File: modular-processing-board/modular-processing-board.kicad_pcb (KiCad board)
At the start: 6 copper layers, 90 x 90 mm, 159 parts, among them J202 Conn_02x06_Odd_Even, J401 Micro_SD_Card, J501 Plug_Hirose_DF40_2x40_DF40C-8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, J502 Conn_02x06_Odd_Even, J601 Conn_Coaxial_Small, J604 Conn_Coaxial_Small, J701 Conn_02x02_Odd_Even, J801 TYPE-C-31-M-12, SW201 SW_Push, SW602 SW_Push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

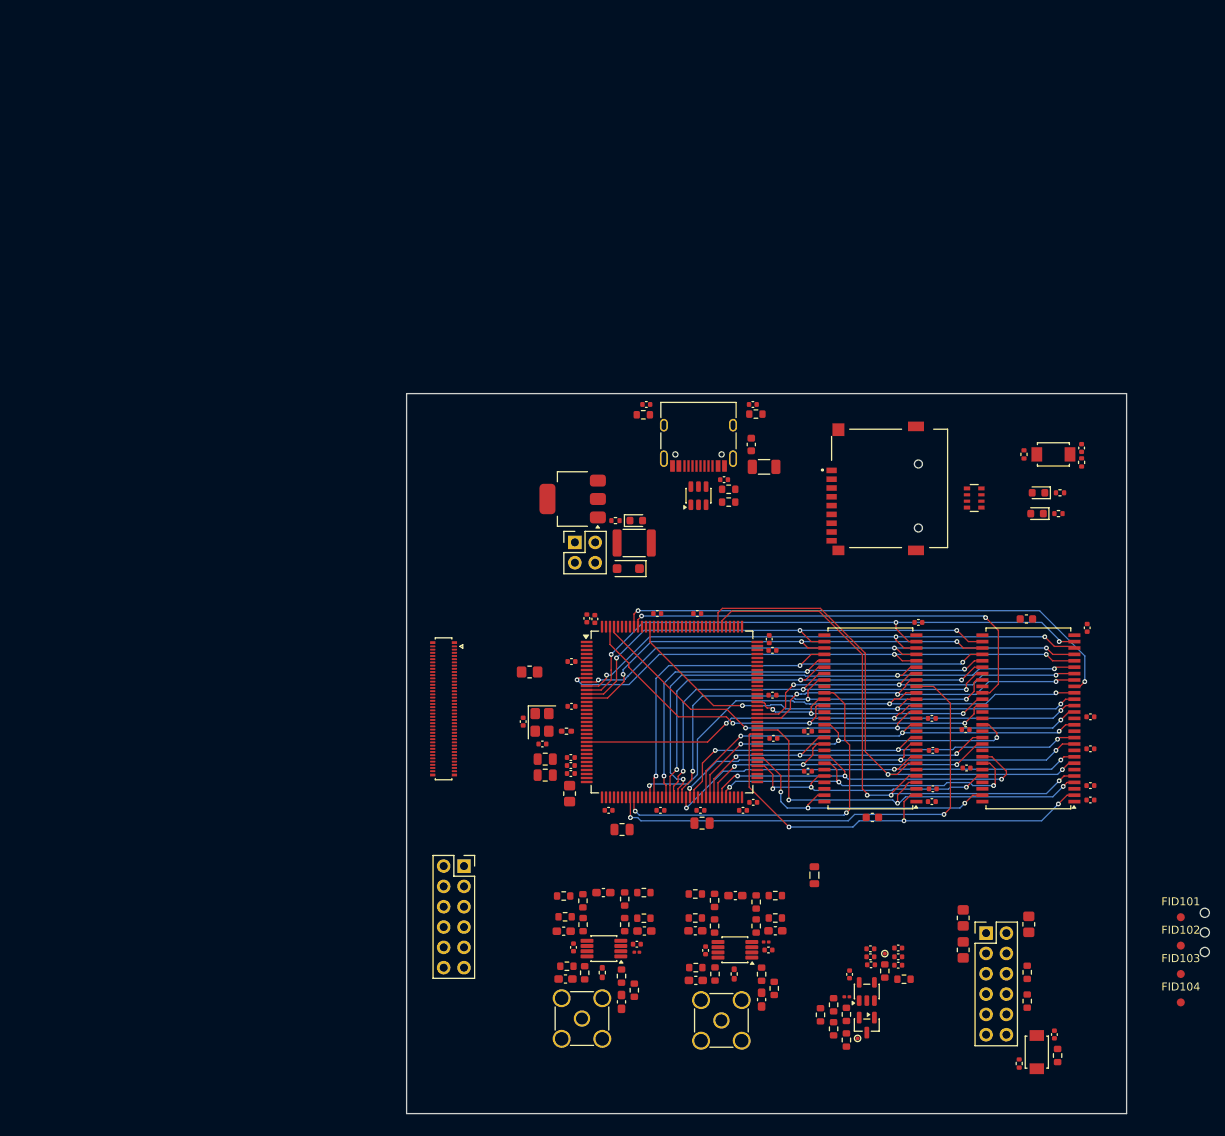
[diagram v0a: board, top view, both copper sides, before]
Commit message: checked timing for sdram, routing
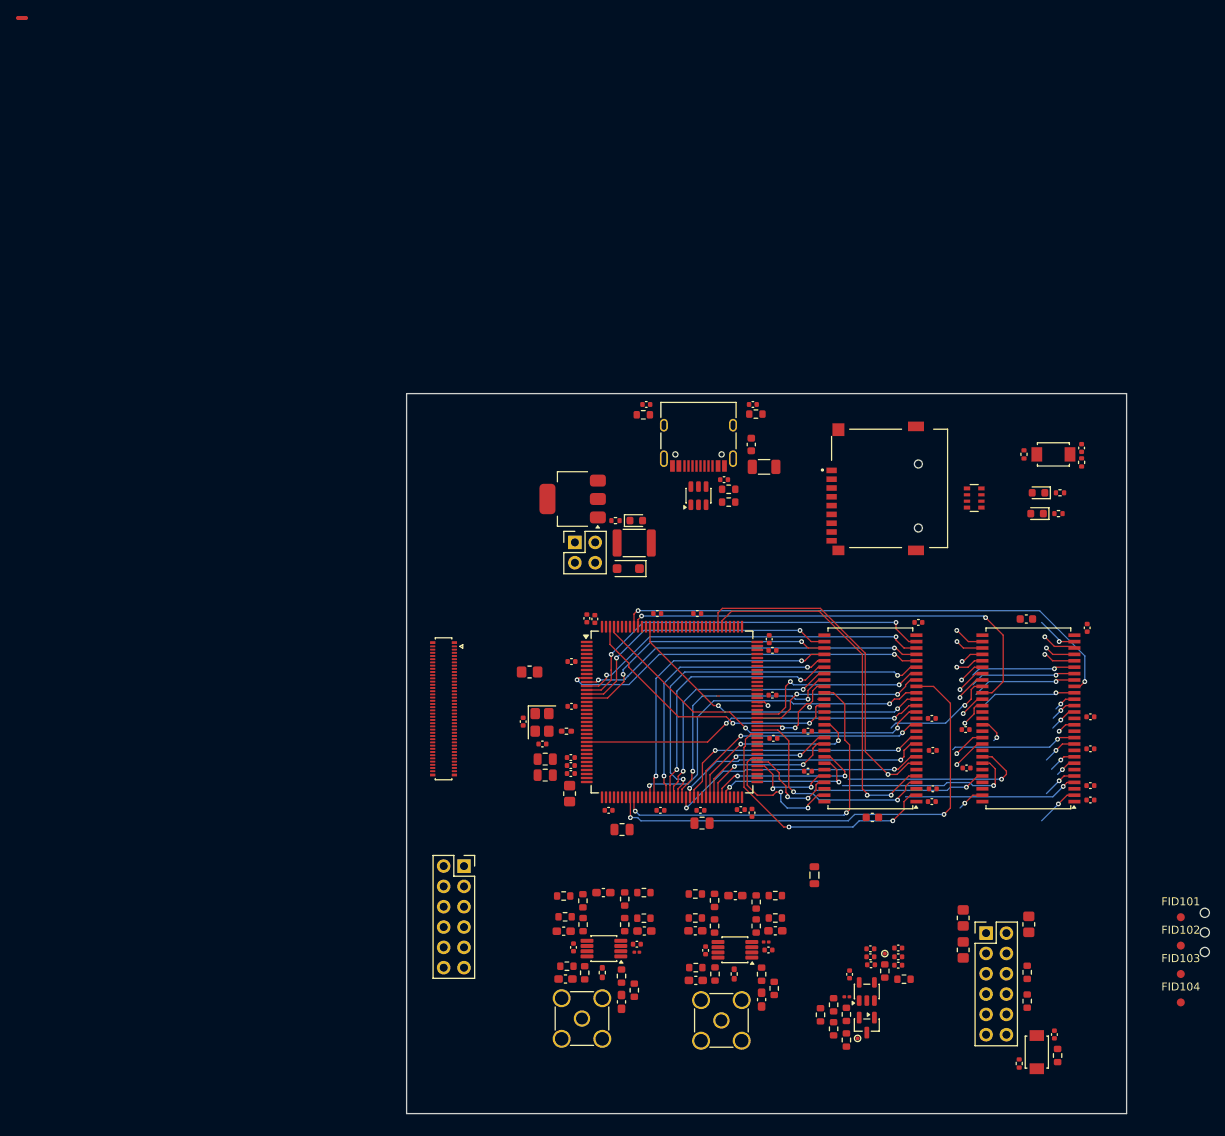
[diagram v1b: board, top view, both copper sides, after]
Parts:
- added NT301: NetTie_2, NetTie:NetTie-2_SMD_Pad0.5mm, F.Cu at (0.75, 0.25)
- moved C211 1.32 mm to (92.0, 99.6), turned to 90 degrees
- moved C222 0.29 mm to (90.6, 99.2)
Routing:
- net /mcu/SDRAM.A12: track 0.00 -> 26.6 mm, vias 0 -> 3
- net /mcu/SDRAM.D3: track 67.0 -> 45.8 mm
- net /mcu/SDRAM.A6: track 60.7 -> 40.3 mm
- net /mcu/SDRAM.A9: track 55.2 -> 35.1 mm
- net /mcu/SDRAM.~{WE}: track 66.3 -> 46.4 mm
- net /mcu/SDRAM.A8: track 56.5 -> 36.7 mm
- net /mcu/SDRAM.A11: track 54.2 -> 34.6 mm
- net /mcu/SDRAM.D4: track 55.9 -> 36.3 mm
- net /mcu/SDRAM.A4: track 58.5 -> 38.9 mm
- net /mcu/SDRAM.~{CAS}: track 61.9 -> 42.3 mm
- net /mcu/SDRAM.D2: track 70.0 -> 50.5 mm
- net /mcu/SDRAM.D8: track 46.5 -> 27.1 mm
- net /mcu/SDRAM.A5: track 56.9 -> 37.5 mm
- net /mcu/SDRAM.D9: track 42.0 -> 22.6 mm
- net /mcu/SDRAM.UDQM: track 58.0 -> 38.6 mm
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
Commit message: rough length mamatching for sdram (next) route PSSI-bus
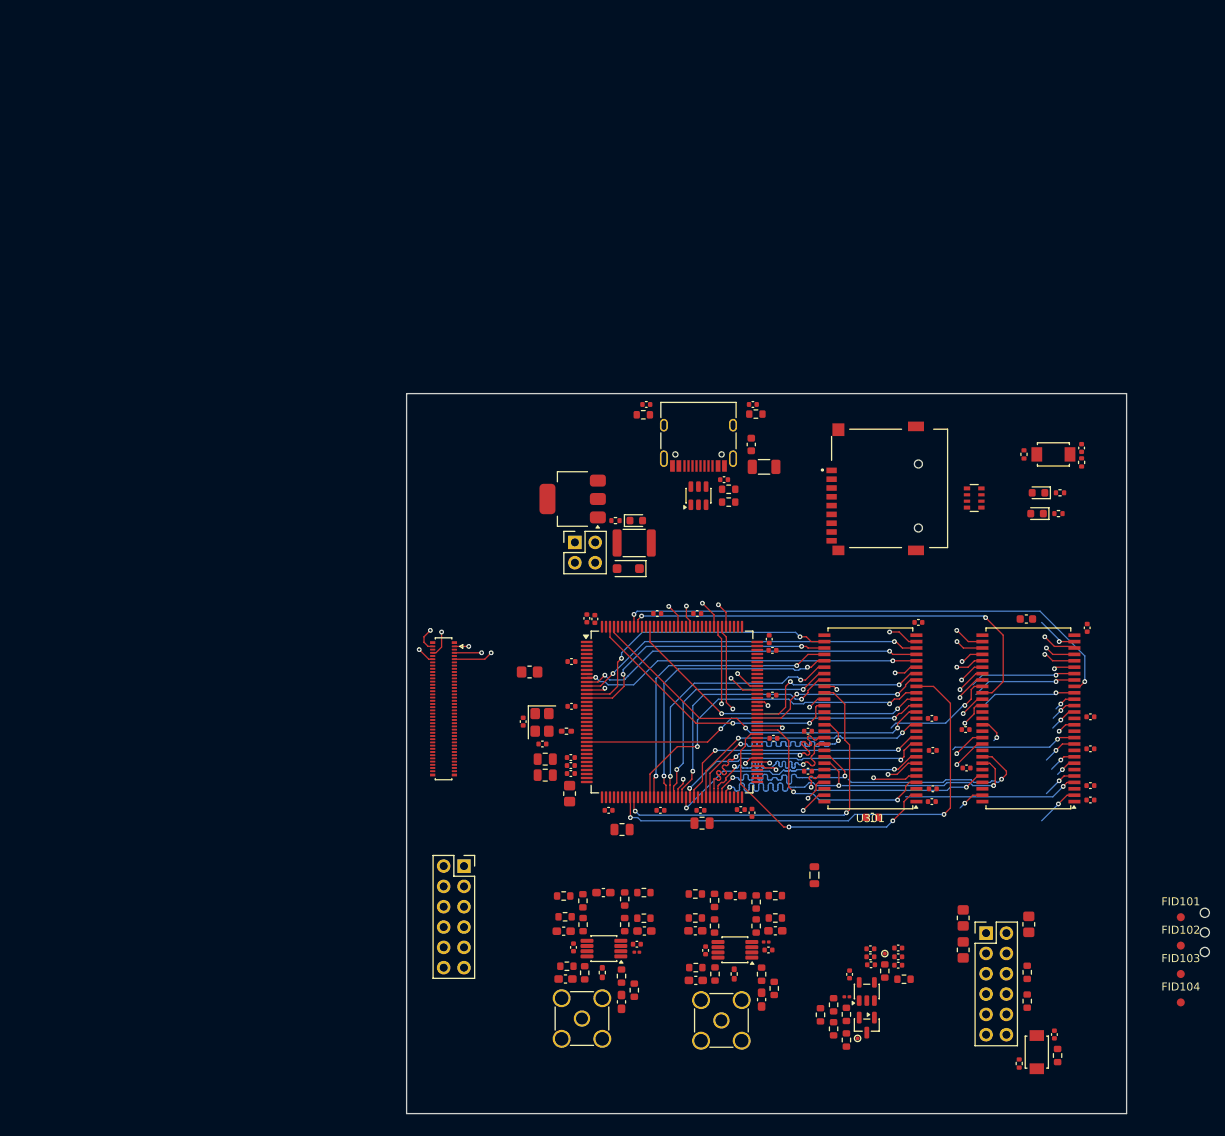
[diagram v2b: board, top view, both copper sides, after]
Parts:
- removed NT301: NetTie_2, NetTie:NetTie-2_SMD_Pad0.5mm
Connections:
- J501 pad 11: Net-(J501-Pad11) -> GND
- J501 pad 12: Net-(J501-Pad12) -> GND
- J501 pad 15: Net-(J501-Pad11) -> GND
- J501 pad 16: Net-(J501-Pad12) -> GND
- J501 pad 19: Net-(J501-Pad11) -> GND
- J501 pad 20: Net-(J501-Pad12) -> GND
- J501 pad 23: Net-(J501-Pad11) -> GND
- J501 pad 24: Net-(J501-Pad12) -> GND
- J501 pad 27: Net-(J501-Pad11) -> GND
- J501 pad 28: Net-(J501-Pad12) -> GND
- J501 pad 3: Net-(J501-Pad11) -> GND
- J501 pad 31: Net-(J501-Pad11) -> GND
- J501 pad 32: Net-(J501-Pad12) -> GND
- J501 pad 35: Net-(J501-Pad11) -> GND
- J501 pad 36: Net-(J501-Pad12) -> GND
- J501 pad 39: Net-(J501-Pad11) -> GND
- J501 pad 4: Net-(J501-Pad12) -> GND
- J501 pad 40: Net-(J501-Pad12) -> GND
- J501 pad 43: Net-(J501-Pad11) -> GND
- J501 pad 44: Net-(J501-Pad12) -> GND
- J501 pad 47: Net-(J501-Pad11) -> GND
- J501 pad 48: Net-(J501-Pad12) -> GND
- J501 pad 7: Net-(J501-Pad11) -> GND
- J501 pad 8: Net-(J501-Pad12) -> GND
- U201 pad 125: unconnected-(U201-PG10-Pad125) -> /connectors/PSSI.D2
- U201 pad 98: /connectors/PSSI.D2 -> unconnected-(U201-PC8-Pad98)
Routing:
- net /connectors/PSSI.D9: track 0.00 -> 44.9 mm, vias 0 -> 2
- net /connectors/PSSI.D11: track 0.00 -> 44.3 mm, vias 0 -> 2
- net /connectors/PSSI.D0: track 0.00 -> 42.3 mm, vias 0 -> 2
- net /connectors/PSSI.D1: track 0.00 -> 41.6 mm, vias 0 -> 2
- net /connectors/PSSI.D10: track 0.00 -> 38.5 mm, vias 0 -> 2
- net /connectors/PSSI.D2: track 0.00 -> 32.5 mm, vias 0 -> 2
- net /mcu/SDRAM.CLK: track 27.4 -> 44.9 mm
- net /mcu/SDRAM.A10: track 60.5 -> 43.4 mm
- net /mcu/SDRAM.D14: track 12.6 -> 28.4 mm
- net /mcu/SDRAM.A12: track 26.6 -> 41.7 mm
- net /mcu/SDRAM.D15: track 20.6 -> 35.6 mm
- net /mcu/SDRAM.D13: track 34.2 -> 48.8 mm
- net /mcu/SDRAM.D10: track 21.9 -> 30.9 mm
- net /mcu/SDRAM.D12: track 42.3 -> 51.1 mm
- net /mcu/SDRAM.D2: track 50.5 -> 42.0 mm
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
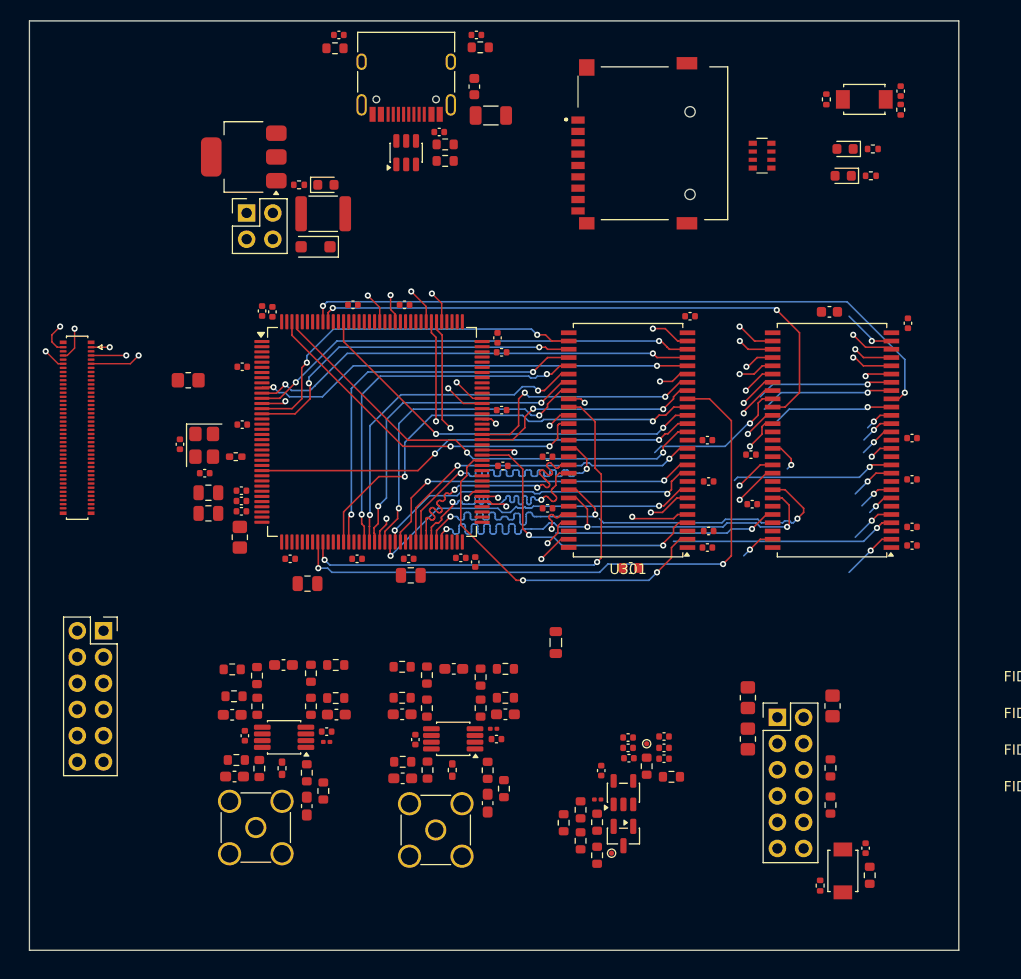
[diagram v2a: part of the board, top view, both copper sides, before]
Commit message: replaced sdmmc connector, added smmc trace, added u.fl. connectors
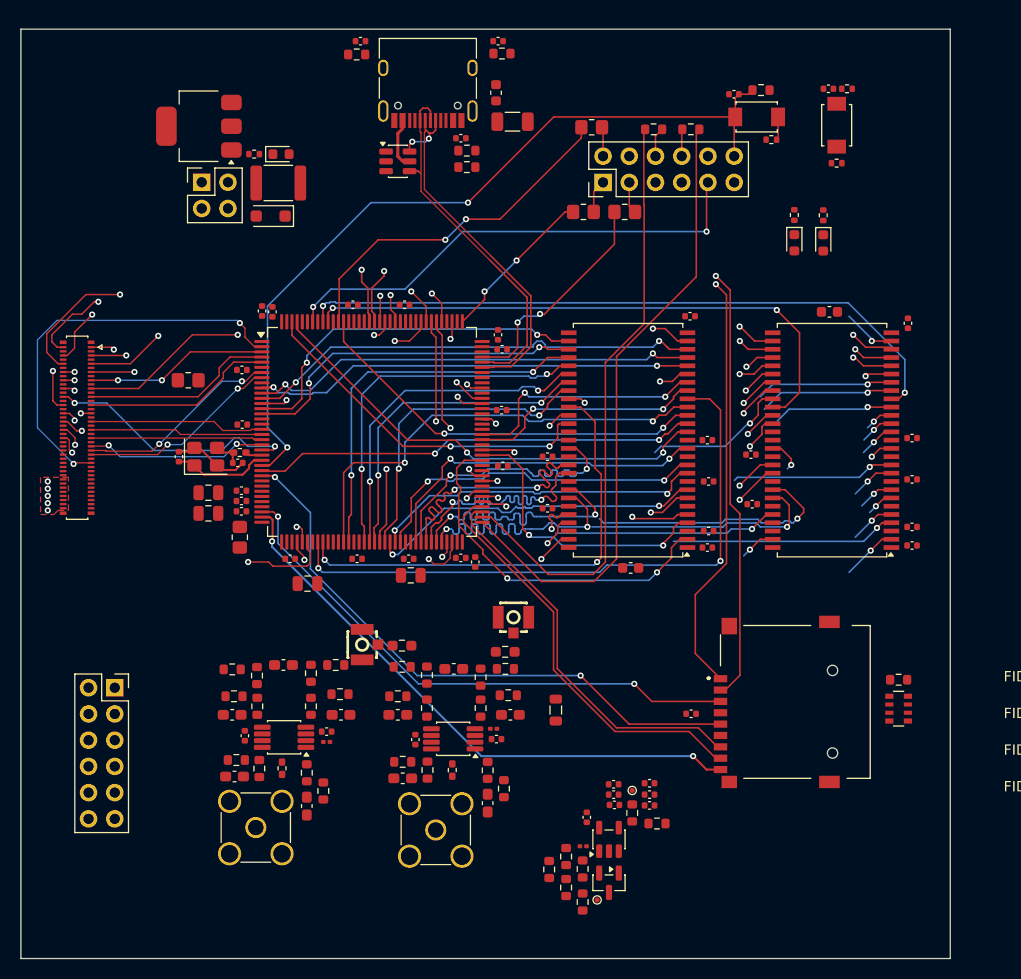
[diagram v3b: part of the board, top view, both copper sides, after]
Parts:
- added C401: 0.1uF, Capacitor_SMD:C_0402_1005Metric, F.Cu at (112.9, 114.3)
- added J1001: BWU.FL-IPEX1, iw-connector:BWU.FL-IPEX1, F.Cu at (95.7, 105.7)
- added J602: BWU.FL-IPEX1, iw-connector:BWU.FL-IPEX1, F.Cu at (81.8, 107.6)
- added R1001: 0, Resistor_SMD:R_0603_1608Metric_Pad0.98x0.95mm_HandSolder, F.Cu at (84.9, 107.7)
- added R401: 10k, Resistor_SMD:R_0603_1608Metric, F.Cu at (133.0, 111.0)
- added R620: 0, Resistor_SMD:R_0603_1608Metric_Pad0.98x0.95mm_HandSolder, F.Cu at (94.9, 108.3)
- J401: value Micro_SD_Card -> TF01A
- moved R208 76.8 mm to (119.7, 53.9), turned to 180 degrees
- moved C216 74.1 mm to (117.0, 54.3), turned to 180 degrees
- moved SW201 73.5 mm to (119.2, 56.5), turned to 0 degrees
- moved R216 72.4 mm to (120.7, 58.7), turned to 180 degrees
- moved R215 66.8 mm to (112.9, 57.7), turned to 180 degrees
- moved R214 64.2 mm to (109.3, 57.7), turned to 0 degrees
- moved R207 60.7 mm to (103.3, 57.5), turned to 0 degrees
- moved J401 55.8 mm to (123.0, 113.2)
- moved RN707 55.2 mm to (133.0, 113.8), turned to 0 degrees
- moved J202 54.5 mm to (104.4, 62.8), turned to 90 degrees
- moved R218 52.4 mm to (106.5, 65.7), turned to 180 degrees
- moved R217 49.7 mm to (102.5, 65.7), turned to 180 degrees
- moved D401 10.3 mm to (122.9, 68.7), turned to -90 degrees
- moved R209 9.94 mm to (122.9, 66.0), turned to -90 degrees
- moved C217 7.00 mm to (126.2, 53.8), turned to 180 degrees
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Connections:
- net /mcu/USB_DM renamed /mcu/USB_DN
- R1006 pad 1: /adc-frontend/ADC_VOCM_BUFF -> /adc-frontend/VOCM_BUFF
- R201 pad 1: VCORE_3V3 -> +3V3
- R608 pad 2: /adc-frontend/ADC_VOCM_BUFF -> /adc-frontend/VOCM_BUFF
- R609 pad 2: /adc-frontend/ADC_VOCM_BUFF -> /adc-frontend/VOCM_BUFF
- R610 pad 2: /adc-frontend/ADC_VOCM_BUFF -> /adc-frontend/VOCM_BUFF
- R612 pad 2: /adc-frontend/ADC_VOCM_BUFF -> /adc-frontend/VOCM_BUFF
- R627 pad 2: /adc-frontend/ADC_VOCM_BUFF -> /adc-frontend/VOCM_BUFF
- R628 pad 1: /adc-frontend/ADC_VOCM_BUFF -> /adc-frontend/VOCM_BUFF
- R629 pad 1: /adc-frontend/ADC_VOCM_BUFF -> /adc-frontend/VOCM_BUFF
- U1002 pad 2: /adc-frontend/ADC_VOCM_BUFF -> /adc-frontend/VOCM_BUFF
- U201 pad 35: unconnected-(U201-PA1-Pad35) -> /mcu/SDMMC.CD
- U603 pad 2: /adc-frontend/ADC_VOCM_BUFF -> /adc-frontend/VOCM_BUFF
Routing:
- net /mcu/SDMMC.D3: track 0.00 -> 82.4 mm, vias 0 -> 2
- net /mcu/SDMMC.D2: track 0.00 -> 80.4 mm, vias 0 -> 2
- net /mcu/MCU_NRST: track 0.00 -> 78.2 mm, vias 0 -> 2
- net /mcu/UART5_RX: track 0.00 -> 61.2 mm
- net /mcu/UART5_TX: track 0.00 -> 58.3 mm
- net /mcu/SDMMC.CK: track 0.00 -> 57.6 mm, vias 0 -> 2
- net /mcu/SDMMC.CD: track 0.00 -> 56.1 mm, vias 0 -> 2
- net /mcu/SDMMC.CMD: track 0.00 -> 53.5 mm, vias 0 -> 2
- net /connectors/PSSI.D8: track 0.00 -> 50.9 mm, vias 0 -> 2
- net /connectors/PSSI.D12: track 0.00 -> 49.9 mm, vias 0 -> 2
- net /mcu/MCU_BOOT0: track 0.00 -> 47.4 mm, vias 0 -> 2
- net /connectors/I2C.SDA: track 0.00 -> 46.7 mm, vias 0 -> 2
- net /connectors/PSSI.D13: track 0.00 -> 46.3 mm, vias 0 -> 2
- net /connectors/I2C.SCL: track 0.00 -> 45.6 mm, vias 0 -> 2
- net /connectors/PSSI.D3: track 0.00 -> 41.0 mm, vias 0 -> 2
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- added copper zone on F.Cu, net /connectors/HRS_3V3
- added copper zone on In3.Cu, net /connectors/HRS_3V3
